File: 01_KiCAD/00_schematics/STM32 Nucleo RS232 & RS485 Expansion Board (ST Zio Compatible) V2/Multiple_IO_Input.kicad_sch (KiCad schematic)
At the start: 10 parts, among them J10 SW ENA, U5 SN74LVC245ADBR

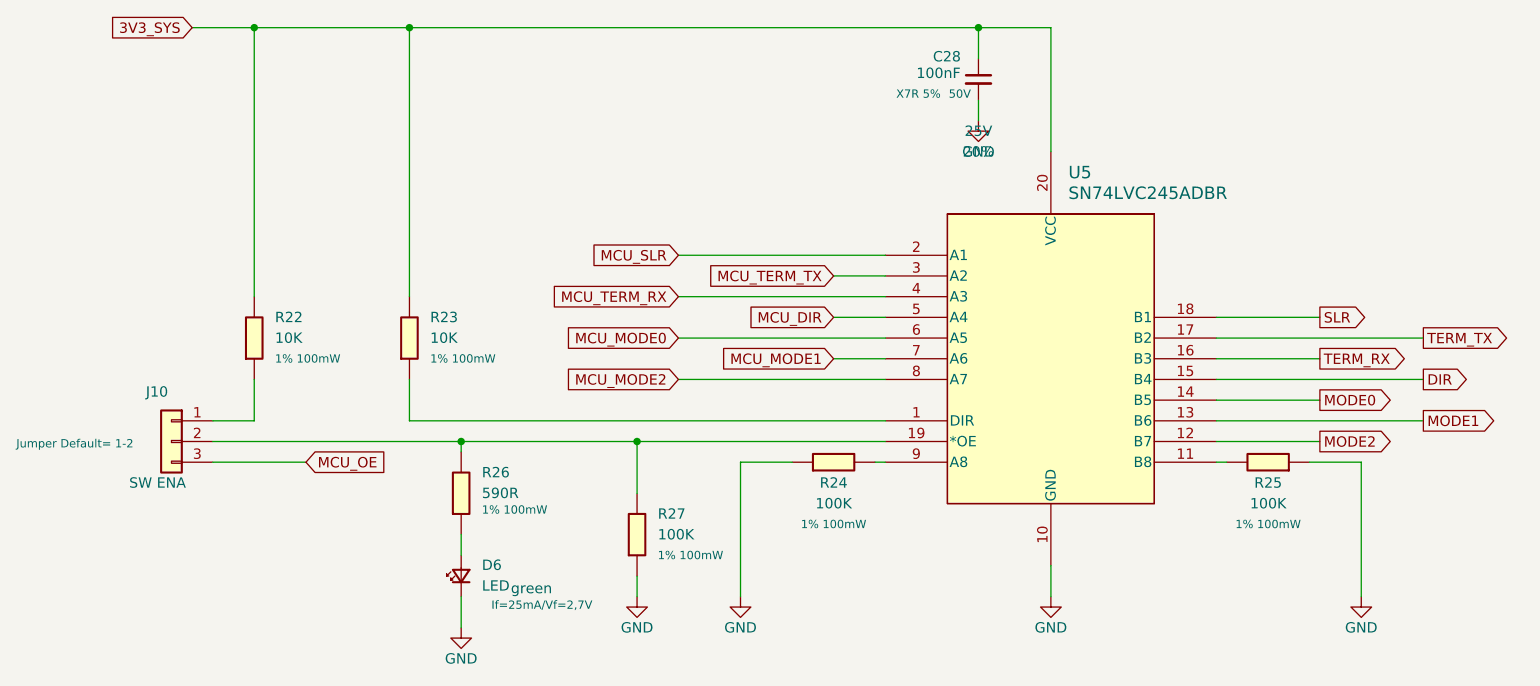
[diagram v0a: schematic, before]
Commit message: Final revision checkup
After BOM-update and corrected some footprints and package sizes for resistors and capacitors, updated the PCB to "HW REV A0.2" as final PCB layout. Need to run DRC check before final approval.
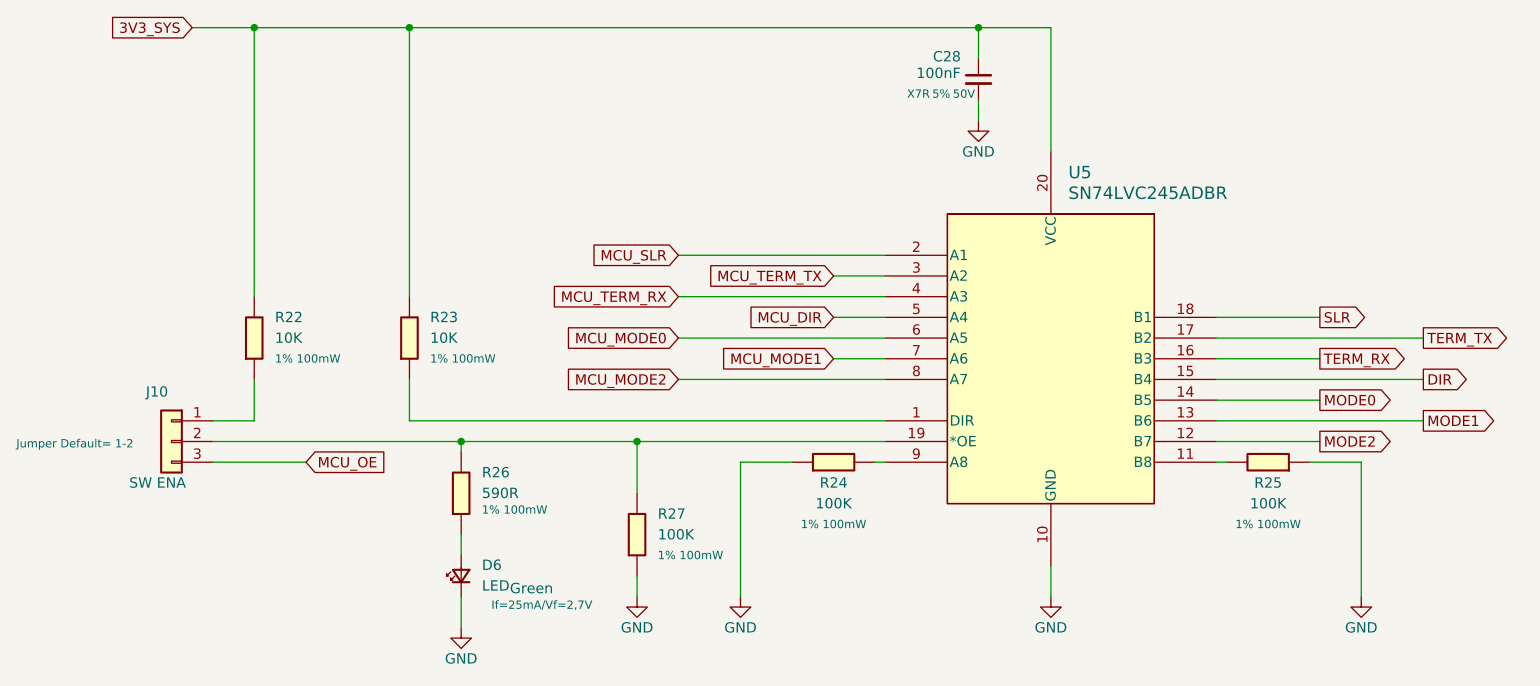
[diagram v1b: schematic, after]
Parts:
- C28: Dielectric X7R 5% -> X7R; LCSC C91183 -> C2167095; MPN CC0603JRX7R9BB104 -> C0805C104J5RACTU; Manufacturer YAGEO -> KEMET; Mouser PN (none) -> 80-C0805C104J5R; Package 0603 -> 0805; Tolerance 20% -> 5%; Voltage 25V -> 50V
- D6: Color green -> Green; Mouser PN (none) -> 743-IN-S63AT5G; Voltage (none) -> 2,7V
- J10: LCSC C6631883 -> C5714562; Mouser PN (none) -> 200-HTSW10307GS
- R22, R23: LCSC C98220 -> C20142011; MPN RC0603FR-0710KL -> AC0603FR-7W10KL; Mouser PN (none) -> 603-AC0603FR-7W10KL
- R24, R25, R27: LCSC C14675 -> C5552302; MPN RC0603FR-07100KL -> AC0603FR-7W100KL; Mouser PN (none) -> 603-AC0603FR-7W100KL
- R26: LCSC C22548 -> C227973; MPN RC0603FR-071KL -> AC0603FR-07590RL; Mouser PN (none) -> 603-AC0603FR-07590RL
- U5: LCSC (none) -> C393617; MPN (none) -> SN74LVC245ADBR; Manufacturer (none) -> TI; Mouser PN (none) -> 595-SN74LVC245ADBR; Package (none) -> SSOP-20; Type (none) -> SMD
